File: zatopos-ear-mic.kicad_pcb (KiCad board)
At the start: 2 copper layers, 80 x 40 mm, 25 parts, among them J2 Conn_01x06_Socket, U1 NJU7043, U2 MCP3002

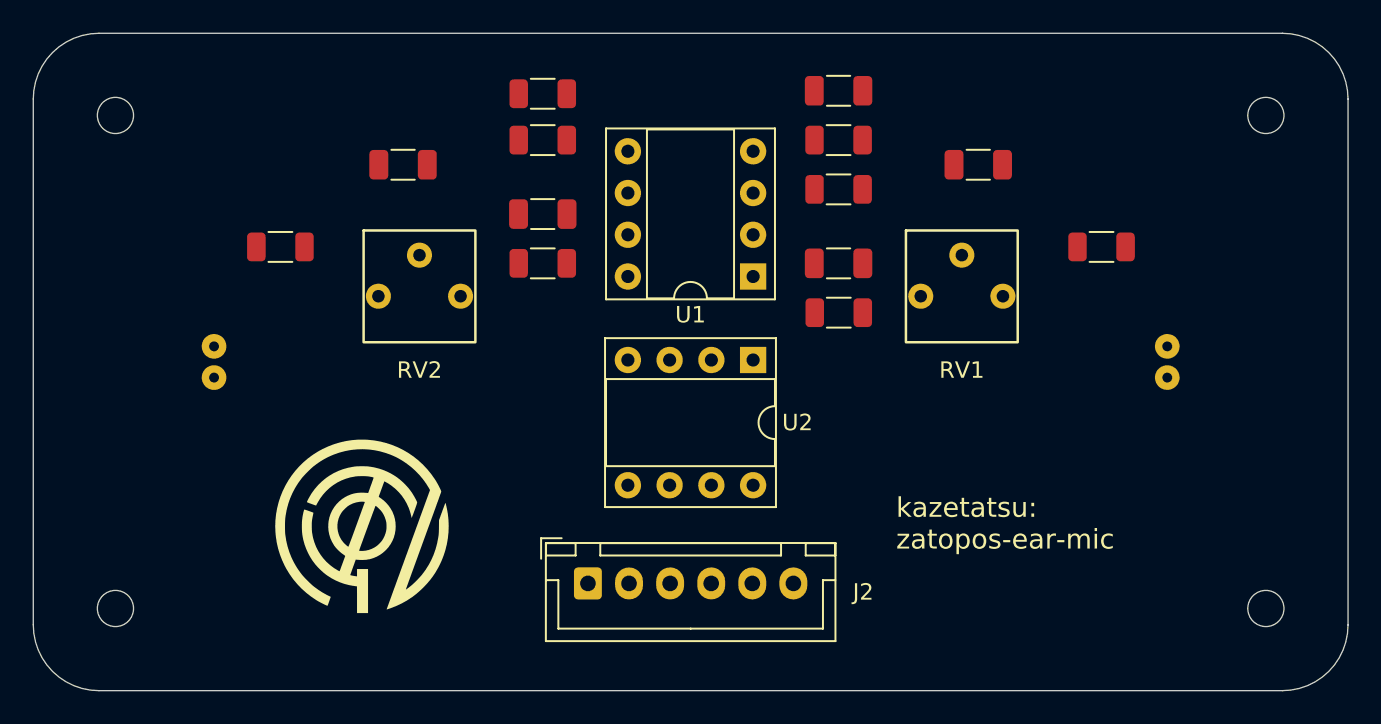
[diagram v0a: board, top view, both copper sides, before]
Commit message: Connect footprints
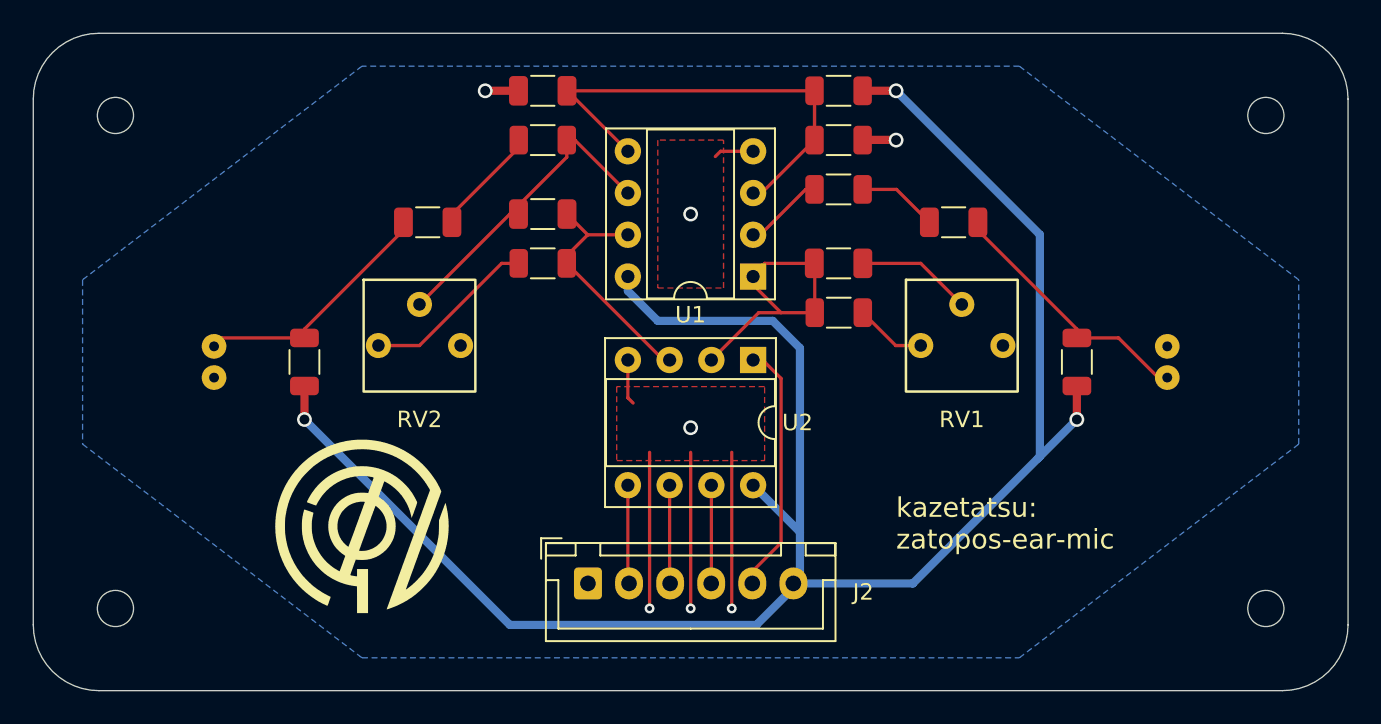
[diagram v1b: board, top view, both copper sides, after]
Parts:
- moved R7 18.0 mm to (159.0, 83.5), turned to 180 degrees
- moved C5 18.0 mm to (141.0, 83.5), turned to 180 degrees
- moved R1 7.16 mm to (173.5, 100.0), turned to -90 degrees
- moved R2 7.15 mm to (126.5, 100.0), turned to 90 degrees
- moved C1 3.81 mm to (166.0, 91.5)
- moved C2 3.81 mm to (134.0, 91.5)
- moved RV1 3.00 mm to (166.5, 99.0)
- moved RV2 3.00 mm to (133.5, 99.0)
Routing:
- net +3.3V: track 0.00 -> 121.0 mm, vias 0 -> 3
- net GND: track 0.00 -> 37.8 mm, vias 0 -> 7
- net OFFSET: track 0.00 -> 28.3 mm
- net Net-(U1-B_IN-): track 0.00 -> 19.1 mm
- net SOUND1: track 0.00 -> 18.2 mm
- net Net-(MIC1-+): track 0.00 -> 16.0 mm
- net Net-(J2-Pin_5): track 0.00 -> 15.4 mm
- net Net-(MIC2-+): track 0.00 -> 15.3 mm
- net SOUND2: track 0.00 -> 15.2 mm
- net Net-(U1-A_IN-): track 0.00 -> 12.2 mm
- net Net-(R6-Pad2): track 0.00 -> 10.6 mm
- net Net-(C2-Pad1): track 0.00 -> 6.68 mm
- net Net-(J2-Pin_2): track 0.00 -> 6.00 mm
- net Net-(J2-Pin_3): track 0.00 -> 5.99 mm
- net Net-(J2-Pin_4): track 0.00 -> 5.98 mm
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- added copper zone on B.Cu, net GND
- added copper zone on F.Cu, net GND

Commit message: Solve errors: not connected
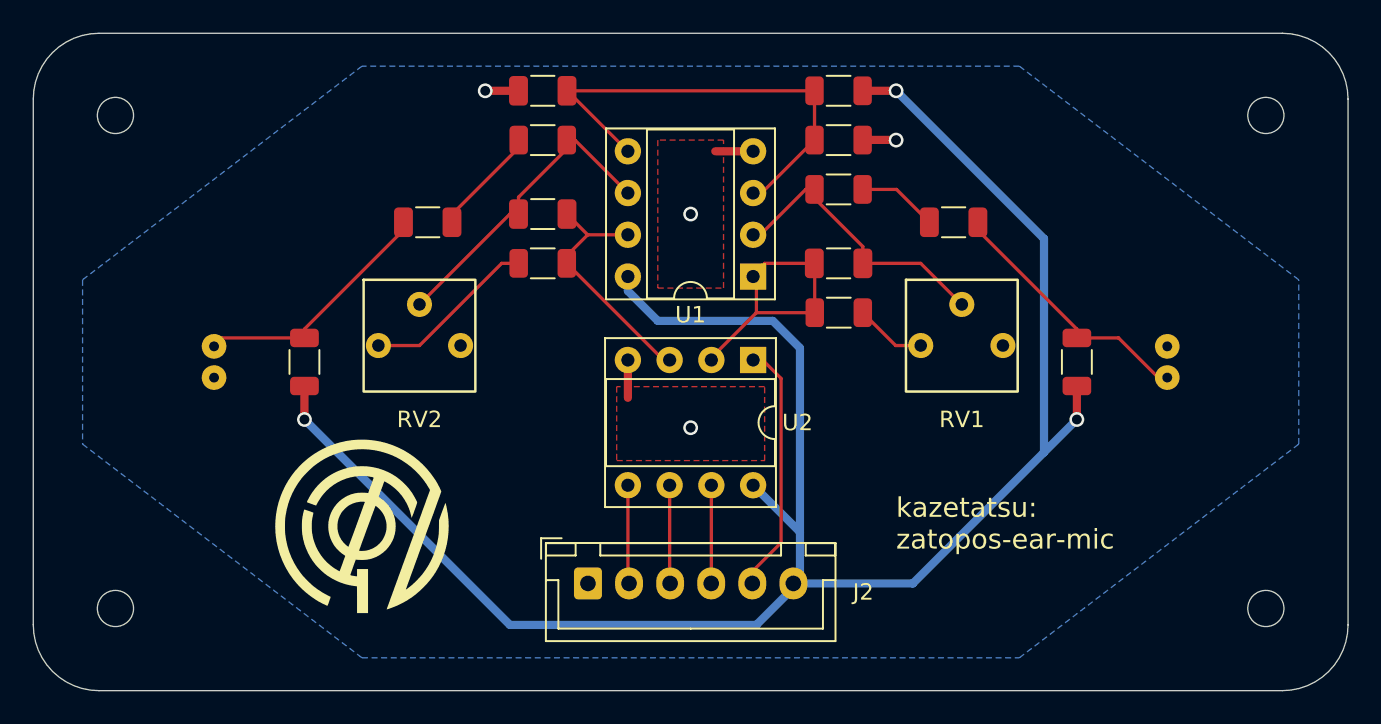
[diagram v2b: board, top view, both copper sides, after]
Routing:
- net GND: track 37.8 -> 8.67 mm, vias 7 -> 4
- net Net-(U1-A_IN-): track 12.2 -> 17.9 mm
- net SOUND1: track 18.2 -> 17.5 mm
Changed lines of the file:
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@@
 		(tags "resistor")
 		(property "Reference" "R7"
-			(at 0 -1.82 360)
+			(at 0 -1.82 0)
 			(layer "F.SilkS")
 			(hide yes)
@@
 		)
 		(property "Value" "100k"
-			(at 0 1.82 360)
+			(at 0 1.82 0)
 			(layer "F.Fab")
 			(effects
@@
 		)
 		(fp_text user "${REFERENCE}"
-			(at 0 0 360)
+			(at 0 0 0)
 			(layer "F.Fab")
 			(effects
@@
 		(tags "capacitor")
 		(property "Reference" "C5"
-			(at 0 -1.85 360)
+			(at 0 -1.85 0)
 			(layer "F.SilkS")
 			(hide yes)
@@
 		)
 		(property "Value" "1u"
-			(at 0 1.85 360)
+			(at 0 1.85 0)
 			(layer "F.Fab")
 			(effects
@@
 		)
 		(fp_text user "${REFERENCE}"
-			(at 0 0 360)
+			(at 0 0 0)
 			(layer "F.Fab")
 			(effects
@@
 	)
 	(segment
-		(start 155.5 97)
-		(end 154.14 97)
+		(start 154 97)
+		(end 154 94.8)
 		(width 0.2)
 		(layer "F.Cu")
@@
 	)
 	(segment
-		(start 153.8 94.8)
-		(end 153.8 95.3)
+		(start 151.26 99.74)
+		(end 151.26 99.88)
 		(width 0.2)
 		(layer "F.Cu")
@@
 	)
 	(segment
-		(start 154.14 97)
-		(end 151.26 99.88)
+		(start 154 97)
+		(end 151.26 99.74)
 		(width 0.2)
 		(layer "F.Cu")
@@
 	)
 	(segment
-		(start 155.5 97)
-		(end 157.55 97)
+		(start 154.5 94)
+		(end 157.525 94)
 		(width 0.2)
 		(layer "F.Cu")
@@
 	)
 	(segment
-		(start 153.8 95.3)
-		(end 155.5 97)
+		(start 157.55 97)
+		(end 154 97)
 		(width 0.2)
 		(layer "F.Cu")
@@
 	)
 	(segment
-		(start 154.5 94)
-		(end 157.525 94)
+		(start 157.5375 89.5)
+		(end 157.5375 90.0375)
 		(width 0.2)
 		(layer "F.Cu")
-		(net 5)
+		(net 6)
+	)
+	(segment
+		(start 157.5375 90.0375)
+		(end 160.475 92.975)
+		(width 0.2)
+		(layer "F.Cu")
+		(net 6)
+	)
+	(segment
+		(start 160.475 92.975)
+		(end 160.475 94)
+		(width 0.2)
+		(layer "F.Cu")
+		(net 6)
 	)
 	(segment
@@
 	(segment
 		(start 139.525 91)
-		(end 139.525 90.525)
+		(end 139.525 89.975)
 		(width 0.2)
 		(layer "F.Cu")
@@
 	)
 	(segment
-		(start 139.5 90.5)
-		(end 142.4625 87.5375)
+		(start 142.96 86.5)
+		(end 142.4625 86.5)
 		(width 0.2)
 		(layer "F.Cu")
@@
 	)
 	(segment
-		(start 142.96 86.5)
+		(start 142.4625 87.0375)
 		(end 142.4625 86.5)
 		(width 0.2)
@@
 	)
 	(segment
-		(start 139.525 90.525)
-		(end 139.5 90.5)
-		(width 0.2)
-		(layer "F.Cu")
-		(net 8)
-	)
-	(segment
-		(start 142.4625 87.5375)
-		(end 142.4625 86.5)
+		(start 139 91)
+		(end 139.525 91)
 		(width 0.2)
 		(layer "F.Cu")
@@
 	)
 	(segment
-		(start 139 91)
-		(end 139.525 91)
+		(start 139.525 89.975)
+		(end 142.4625 87.0375)
 		(width 0.2)
 		(layer "F.Cu")
@@
 	)
 	(segment
-		(start 153.8 87.18)
-		(end 151.82 87.18)
-		(width 0.2)
-		(layer "F.Cu")
-		(net 9)
-	)
-	(segment
-		(start 146.18 102.18)
-		(end 146.5 102.5)
-		(width 0.2)
-		(layer "F.Cu")
-		(net 9)
-	)
-	(segment
 		(start 160.475 86.4875)
 		(end 162.4875 86.4875)
@@
 	)
 	(segment
-		(start 150 105.5)
-		(end 150 115)
-		(width 0.2)
-		(layer "F.Cu")
-		(net 9)
-	)
-	(segment
-		(start 151.82 87.18)
-		(end 151.5 87.5)
-		(width 0.2)
-		(layer "F.Cu")
-		(net 9)
-	)
-	(segment
 		(start 162.4875 86.4875)
 		(end 162.5 86.5)
@@
 	)
 	(segment
-		(start 160.475 86.4875)
-		(end 160.4625 86.5)
-		(width 0.2)
-		(layer "F.Cu")
-		(net 9)
-	)
-	(segment
-		(start 152.5 105.5)
-		(end 152.5 115)
-		(width 0.2)
+		(start 153.8 87.18)
+		(end 151.5 87.18)
+		(width 0.5)
 		(layer "F.Cu")
 		(net 9)
 	)
 	(segment
-		(start 147.5 105.5)
-		(end 147.5 115)
+		(start 160.475 86.4875)
+		(end 160.4625 86.5)
 		(width 0.2)
 		(layer "F.Cu")
@@
 		(start 146.18 99.88)
 		(end 146.18 102.18)
-		(width 0.2)
+		(width 0.5)
 		(layer "F.Cu")
 		(net 9)
 	)
 	(via
-		(at 150 115)
-		(size 0.6)
-		(drill 0.3)
-		(layers "F.Cu" "B.Cu")
-		(free yes)
-		(net 9)
-	)
-	(via
 		(at 137.5 83.5)
 		(size 0.9)
@@
 	)
 	(via
-		(at 152.5 115)
-		(size 0.6)
-		(drill 0.3)
-		(layers "F.Cu" "B.Cu")
-		(free yes)
-		(net 9)
-	)
-	(via
 		(at 162.5 86.5)
 		(size 0.9)
@@
 	)
 	(via
-		(at 147.5 115)
-		(size 0.6)
-		(drill 0.3)
-		(layers "F.Cu" "B.Cu")
-		(free yes)
-		(net 9)
-	)
-	(via
 		(at 150 104)
 		(size 0.9)
@@
 	)
 	(segment
-		(start 156.65 113.075)
-		(end 156.25 113.475)
+		(start 162.5 83.5)
+		(end 171.5 92.5)
 		(width 0.5)
 		(layer "B.Cu")
@@
 	)
 	(segment
-		(start 156.65 110.35)
-		(end 156.65 99.15)
+		(start 156.65 113.075)
+		(end 156.25 113.475)
 		(width 0.5)
 		(layer "B.Cu")
@@
 	)
 	(segment
-		(start 162.5 83.5)
-		(end 171.25 92.25)
+		(start 156.65 110.35)
+		(end 156.65 99.15)
 		(width 0.5)
 		(layer "B.Cu")
@@
 	)
 	(segment
-		(start 171.25 92.25)
-		(end 171.25 105.75)
-		(width 0.5)
-		(layer "B.Cu")
-		(net 14)
-	)
-	(segment
 		(start 153.8 107.5)
 		(end 156.65 110.35)
@@
 	)
 	(segment
-		(start 171.25 105.75)
-		(end 171.125 105.875)
+		(start 154 116)
+		(end 139 116)
 		(width 0.5)
 		(layer "B.Cu")
@@
 	)
 	(segment
-		(start 154 116)
-		(end 139 116)
+		(start 171.5 92.5)
+		(end 171.5 105.5)
 		(width 0.5)
 		(layer "B.Cu")
@@
 		(min_thickness 0.25)
 		(filled_areas_thickness no)
-		(fill
+		(fill yes
 			(thermal_gap 0.5)
 			(thermal_bridge_width 0.5)
@@
 		(min_thickness 0.25)
 		(filled_areas_thickness no)
-		(fill
+		(fill yes
 			(thermal_gap 0.5)
 			(thermal_bridge_width 0.5)
@@
 		(min_thickness 0.25)
 		(filled_areas_thickness no)
-		(fill
+		(fill yes
 			(thermal_gap 0.5)
 			(thermal_bridge_width 0.5)

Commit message: Small change place
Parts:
- moved C5 3.50 mm to (144.5, 83.5)
- moved R5 0.50 mm to (159.0, 96.5)
- moved C3 0.50 mm to (159.0, 93.5)
- moved C4 0.50 mm to (141.0, 90.5)
- moved R6 0.50 mm to (141.0, 93.5)
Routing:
- net OFFSET: track 28.3 -> 23.4 mm
- net SOUND1: track 17.5 -> 13.9 mm
- net SOUND2: track 15.2 -> 15.7 mm
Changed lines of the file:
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@@
 	(footprint "Capacitor_SMD:C_1206_3216Metric"
 		(layer "F.Cu")
-		(at 159 94)
+		(at 159 93.5)
 		(descr "Capacitor SMD 1206 (3216 Metric), square (rectangular) end terminal, IPC_7351 nominal, (Body size source: IPC-SM-782 page 76, https://www.pcb-3d.com/wordpress/wp-content/uploads/ipc-sm-782a_amendment_1_and_2.pdf), generated with kicad-footprint-generator")
 		(tags "capacitor")
@@
 	(footprint "Resistor_SMD:R_1206_3216Metric"
 		(layer "F.Cu")
-		(at 141 94 180)
+		(at 141 93.5 180)
 		(descr "Resistor SMD 1206 (3216 Metric), square (rectangular) end terminal, IPC_7351 nominal, (Body size source: IPC-SM-782 page 72, https://www.pcb-3d.com/wordpress/wp-content/uploads/ipc-sm-782a_amendment_1_and_2.pdf), generated with kicad-footprint-generator")
 		(tags "resistor")
@@
 	(footprint "Resistor_SMD:R_1206_3216Metric"
 		(layer "F.Cu")
-		(at 159.0125 97 180)
+		(at 159 96.5 180)
 		(descr "Resistor SMD 1206 (3216 Metric), square (rectangular) end terminal, IPC_7351 nominal, (Body size source: IPC-SM-782 page 72, https://www.pcb-3d.com/wordpress/wp-content/uploads/ipc-sm-782a_amendment_1_and_2.pdf), generated with kicad-footprint-generator")
 		(tags "resistor")
@@
 	(footprint "Capacitor_SMD:C_1206_3216Metric"
 		(layer "F.Cu")
-		(at 141 83.5 180)
+		(at 144.5 83.5 180)
 		(descr "Capacitor SMD 1206 (3216 Metric), square (rectangular) end terminal, IPC_7351 nominal, (Body size source: IPC-SM-782 page 76, https://www.pcb-3d.com/wordpress/wp-content/uploads/ipc-sm-782a_amendment_1_and_2.pdf), generated with kicad-footprint-generator")
 		(tags "capacitor")
@@
 	(footprint "Capacitor_SMD:C_1206_3216Metric"
 		(layer "F.Cu")
-		(at 141 91 180)
+		(at 141 90.5 180)
 		(descr "Capacitor SMD 1206 (3216 Metric), square (rectangular) end terminal, IPC_7351 nominal, (Body size source: IPC-SM-782 page 76, https://www.pcb-3d.com/wordpress/wp-content/uploads/ipc-sm-782a_amendment_1_and_2.pdf), generated with kicad-footprint-generator")
 		(tags "capacitor")
@@
 	)
 	(segment
-		(start 157.55 97)
-		(end 157.55 94.025)
+		(start 155.8375 94.8)
+		(end 157.1375 93.5)
 		(width 0.2)
 		(layer "F.Cu")
@@
 	)
 	(segment
-		(start 154 94.5)
-		(end 154.5 94)
+		(start 153.8 94.8)
+		(end 154 94.6)
 		(width 0.2)
 		(layer "F.Cu")
@@
 	(segment
 		(start 153.8 94.8)
-		(end 154 94.6)
+		(end 155.8375 94.8)
 		(width 0.2)
 		(layer "F.Cu")
@@
 	)
 	(segment
-		(start 154 97)
-		(end 154 94.8)
+		(start 155.8375 94.8)
+		(end 157.5375 96.5)
 		(width 0.2)
 		(layer "F.Cu")
@@
 	)
 	(segment
-		(start 151.26 99.74)
-		(end 151.26 99.88)
-		(width 0.2)
-		(layer "F.Cu")
-		(net 5)
-	)
-	(segment
-		(start 154 97)
-		(end 151.26 99.74)
+		(start 153.8 94.8)
+		(end 153.8 97.34)
 		(width 0.2)
 		(layer "F.Cu")
@@
 	)
 	(segment
-		(start 154.5 94)
-		(end 157.525 94)
+		(start 153.8 97.34)
+		(end 151.26 99.88)
 		(width 0.2)
 		(layer "F.Cu")
@@
 	)
 	(segment
-		(start 157.55 97)
-		(end 154 97)
+		(start 157.1375 93.5)
+		(end 157.525 93.5)
 		(width 0.2)
 		(layer "F.Cu")
@@
 	)
 	(segment
-		(start 142.4625 94)
+		(start 146.18 92.26)
+		(end 144.235 92.26)
+		(width 0.2)
+		(layer "F.Cu")
+		(net 7)
+	)
+	(segment
+		(start 148.72 99.88)
 		(end 148.3425 99.88)
 		(width 0.2)
@@
 	)
 	(segment
-		(start 142.4625 93.5325)
-		(end 143.735 92.26)
+		(start 144.235 92.26)
+		(end 144.235 92.265)
 		(width 0.2)
 		(layer "F.Cu")
@@
 	)
 	(segment
-		(start 148.3425 99.88)
-		(end 148.72 99.88)
+		(start 142.4625 94)
+		(end 142.4625 93.5)
 		(width 0.2)
 		(layer "F.Cu")
@@
 	(segment
 		(start 142.475 91)
-		(end 143.735 92.26)
+		(end 142.975 91)
 		(width 0.2)
 		(layer "F.Cu")
@@
 	)
 	(segment
-		(start 143.735 92.26)
-		(end 146.18 92.26)
+		(start 148.3425 99.88)
+		(end 142.4625 94)
 		(width 0.2)
 		(layer "F.Cu")
@@
 	)
 	(segment
-		(start 142.4625 94)
-		(end 142.4625 93.5325)
+		(start 142.975 91)
+		(end 144.235 92.26)
+		(width 0.2)
+		(layer "F.Cu")
+		(net 7)
+	)
+	(segment
+		(start 144.235 92.265)
+		(end 143 93.5)
+		(width 0.2)
+		(layer "F.Cu")
+		(net 7)
+	)
+	(segment
+		(start 143 93.5)
+		(end 142.4625 93.5)
 		(width 0.2)
 		(layer "F.Cu")
@@
 	)
 	(segment
-		(start 139.525 83.5)
-		(end 137.5 83.5)
-		(width 0.5)
-		(layer "F.Cu")
-		(net 9)
-	)
-	(segment
 		(start 153.8 87.18)
 		(end 151.5 87.18)
@@
 		(net 9)
 	)
+	(segment
+		(start 143.0125 83.5)
+		(end 140.9875 83.5)
+		(width 0.5)
+		(layer "F.Cu")
+		(net 9)
+	)
 	(via
-		(at 137.5 83.5)
+		(at 140.9875 83.5)
 		(size 0.9)
 		(drill 0.6)
@@
 	)
 	(segment
-		(start 157.5375 83.5)
-		(end 142.475 83.5)
+		(start 154.3175 89.72)
+		(end 153.8 89.72)
 		(width 0.2)
 		(layer "F.Cu")
@@
 	(segment
 		(start 146.18 87.18)
-		(end 142.68 83.68)
+		(end 146.18 83.705)
 		(width 0.2)
 		(layer "F.Cu")
@@
 	)
 	(segment
-		(start 154.3175 89.72)
-		(end 153.8 89.72)
+		(start 157.5375 83.5)
+		(end 145.975 83.5)
 		(width 0.2)
 		(layer "F.Cu")
@@
 	)
 	(segment
-		(start 142.68 83.68)
-		(end 142.4625 83.68)
+		(start 146.18 83.705)
+		(end 145.975 83.5)
 		(width 0.2)
 		(layer "F.Cu")
@@
 	)
 	(segment
-		(start 162.475 99)
-		(end 160.475 97)
+		(start 164 99)
+		(end 161.5 96.5)
 		(width 0.2)
 		(layer "F.Cu")
@@
 	)
 	(segment
-		(start 164 99)
-		(end 162.475 99)
+		(start 161.5 96.5)
+		(end 160.4625 96.5)
 		(width 0.2)
 		(layer "F.Cu")
@@
 	)
 	(segment
-		(start 133.5 99)
-		(end 138.5 94)
+		(start 139 93.5)
+		(end 139.5375 93.5)
 		(width 0.2)
 		(layer "F.Cu")
@@
 	)
 	(segment
-		(start 138.5 94)
-		(end 139.5375 94)
+		(start 133.5 99)
+		(end 139 93.5)
 		(width 0.2)
 		(layer "F.Cu")
